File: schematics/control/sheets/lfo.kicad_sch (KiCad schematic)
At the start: 33 parts, among them Q1 BC548C, Q2 BC548C, U1 TL074, U10 TL072, U2 TL072, U9 TL074

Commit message: Added pulse width mod schematics
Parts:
- removed C18: 22n-47n (foil), Capacitor_THT:C_Rect_L7.0mm_W2.5mm_P5.00mm, symbol Device:C
- removed Q2: BC548C, Package_TO_SOT_THT:TO-92L_Inline_Wide, symbol Transistor_BJT:BC548
- removed R18, R19, R21, R23, R25: 100k, Shmoergh_Custom_Footprints:R_Axial_DIN0207_L6.3mm_D2.5mm_P7.62mm_Horizontal, symbol Device:R
- removed R27: 10k, Shmoergh_Custom_Footprints:R_Axial_DIN0207_L6.3mm_D2.5mm_P7.62mm_Horizontal, symbol Device:R
- removed R29, R31: 47k, Shmoergh_Custom_Footprints:R_Axial_DIN0207_L6.3mm_D2.5mm_P7.62mm_Horizontal, symbol Device:R
- removed R33: 1k, Shmoergh_Custom_Footprints:R_Axial_DIN0207_L6.3mm_D2.5mm_P7.62mm_Horizontal, symbol Device:R
- removed RV_PWM_SPEED1: R_Potentiometer_Trim, Potentiometer_THT:Potentiometer_Runtron_RM-065_Vertical, symbol Device:R_Potentiometer_Trim
- removed U1: TL074, Package_DIP:DIP-14_W7.62mm, symbol Amplifier_Operational:TL074
- removed U10, U2: TL072, Package_DIP:DIP-8_W7.62mm, symbol Amplifier_Operational:TL072
- added C29: 470n foil, symbol Device:C
- added R1 (x2): 47k, symbol Device:R
- added R49: 100k, symbol Device:R
- added R50: 220k, symbol Device:R
- added RV1 (x2): 100k, symbol Device:R_Potentiometer_Trim
- added RV_PWM_FREQ2: 1M, symbol Device:R_Potentiometer_Trim
- added SW1: SW_DP3T, symbol Switch:SW_DP3T
- added U11: TL072, symbol Amplifier_Operational:TL072
- added unit 4 of U7
- added unit 3 of U7
- renumbered C13 to C12, C14 to C13, C15 to C14, C16 to C15, C17 to C16, R16 to R29, R17 to R30, R20 to R31, R22 to R32, R24 to R33, R26 to R34, R28 to R35, R30 to R36, R32 to R37, RV_LFO_SPEED2 to RV_LFO_SPEED1, U9 to U7
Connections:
- net +12V: now also R1.2, R1.2, U11.8 (V+)
- net -12V: now also U11.4 (V-)
- net GND: now also RV1.1, RV1.1, SW1.1, SW1.5, SW1.6, U11.3 (+), U11.6 (-), U7.12 (+)
- net PWM_OUT: now also SW1.7
- net at C16.1, U7.1, U7.6 (-): now also U7.10 (+)
- net at R37.2: now also U7.8, U7.9 (-)
- new net: R1.1, RV1.3 (x2)
- new net: RV1.2, SW1.4
- new net: R49.2, R50.1, U11.5 (+)
- new net: R50.2, RV_PWM_FREQ2.2, RV_PWM_FREQ2.3, U11.7
- new net: C29.1, RV_PWM_FREQ2.1, U11.2 (-)
- new net: U7.13 (-), U7.14
- new net: C29.2, R49.1, SW1.8, U11.1
- new net: RV1.2, SW1.2
- new net PULSE_WIDTH: SW1.3
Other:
- note added: "PWM positions: 1. Square 2. Narrow 3. PWM"
- note removed: "The other half of the LFO is in the filter LFO sheet. Should be close to each other on the PCB."
- moved on the sheet: C12, C13, C14, C15, U7E

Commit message: Updated PWM values
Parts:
- added R52: 100k-1M, symbol Device:R
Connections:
- net at R50.2, U11.7: now also R52.2; no longer RV_PWM_FREQ2.2, RV_PWM_FREQ2.3
- new net: R52.1, RV_PWM_FREQ2.2, RV_PWM_FREQ2.3
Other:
- note added: "Slowing PWM even further down"
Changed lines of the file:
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@@
   (junction (at 63.5 172.72) (diameter 0) (color 0 0 0 0)
   )
+  (junction (at 158.75 114.3) (diameter 0) (color 0 0 0 0)
+  )
   (junction (at 36.83 172.72) (diameter 0) (color 0 0 0 0)
   )
@@
   (junction (at 128.27 67.31) (diameter 0) (color 0 0 0 0)
   )
-  (junction (at 158.75 114.3) (diameter 0) (color 0 0 0 0)
-  )
   (junction (at 76.2 180.34) (diameter 0) (color 0 0 0 0)
   )
@@
     (stroke (width 0) (type default))
   )
+  (wire (pts (xy 175.26 114.3) (xy 186.69 114.3))
+    (stroke (width 0) (type default))
+  )
   (wire (pts (xy 86.36 41.91) (xy 99.06 41.91))
     (stroke (width 0) (type default))
@@
     (stroke (width 0) (type default))
   )
+  (wire (pts (xy 158.75 114.3) (xy 167.64 114.3))
+    (stroke (width 0) (type default))
+  )
   (wire (pts (xy 176.53 46.99) (xy 172.72 46.99))
     (stroke (width 0) (type default))
@@
     (stroke (width 0) (type default))
   )
+  (polyline (pts (xy 171.45 102.87) (xy 171.45 107.95))
+    (stroke (width 0) (type dash))
+  )
   (wire (pts (xy 236.22 128.27) (xy 241.3 128.27))
     (stroke (width 0) (type default))
@@
   )
   (wire (pts (xy 236.22 118.11) (xy 241.3 118.11))
-    (stroke (width 0) (type default))
-  )
-  (wire (pts (xy 158.75 114.3) (xy 186.69 114.3))
     (stroke (width 0) (type default))
   )
@@
   )
   (text "PWM positions:\n1. Square\n2. Narrow\n3. PWM" (at 241.3 148.59 0)
+    (effects (font (size 1.27 1.27)) (justify left bottom))
+  )
+  (text "Slowing PWM even further down" (at 149.86 101.6 0)
     (effects (font (size 1.27 1.27)) (justify left bottom))
   )
@@
         )
       )
+    )
+  )
+  (symbol (lib_id "Device:R") (at 171.45 114.3 90) (unit 1)
+    (in_bom yes) (on_board yes) (dnp no) (fields_autoplaced)
+    (property "Reference" "R52" (at 171.45 109.22 90)
+      (effects (font (size 1.27 1.27)))
+    )
+    (property "Value" "100k-1M" (at 171.45 111.76 90)
+      (effects (font (size 1.27 1.27)))
+    )
+    (property "Footprint" "" (at 171.45 116.078 90)
+      (effects (font (size 1.27 1.27)) hide)
+    )
+    (property "Datasheet" "~" (at 171.45 114.3 0)
+      (effects (font (size 1.27 1.27)) hide)
+    )
+    (pin "1")
+    (pin "2")
+    (instances
+      (project "shmoergh-funk-live-control"
+        (path "/6d7b782d-8b2e-4b40-a99f-4bf41187d978/2e981da9-3fd3-40a6-a1fb-543bdfad6423"
+          (reference "R52") (unit 1)
+        )
+      )

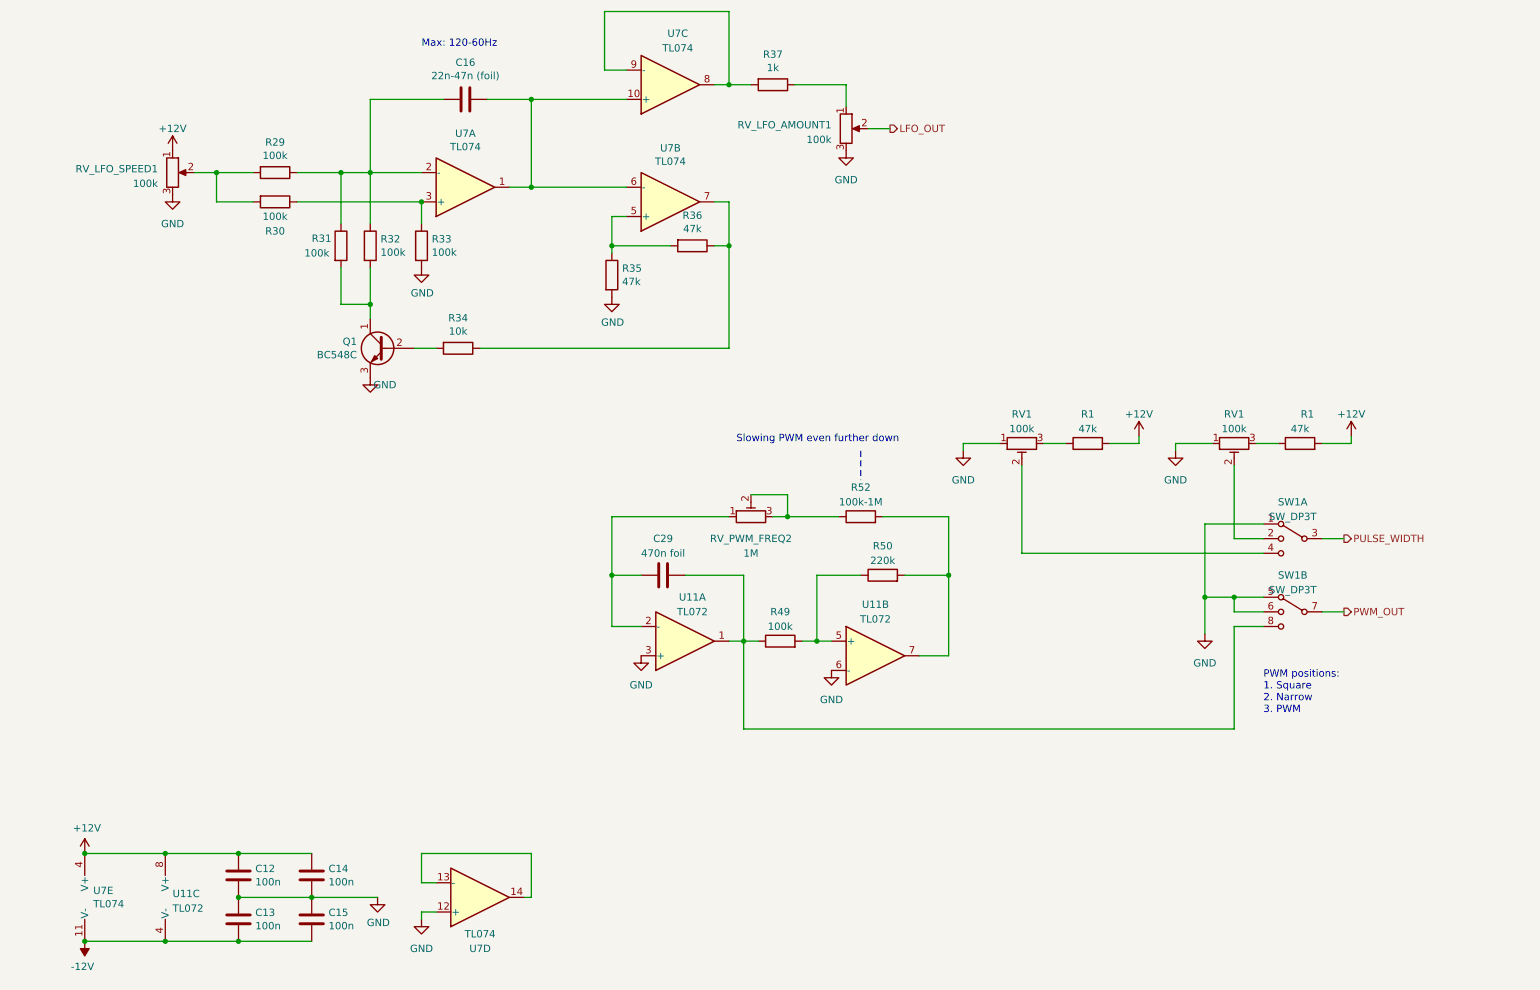
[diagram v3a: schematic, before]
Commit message: Added all UI components to schematics
- digital UI
- filter UI
- updated voice interface connection
- simplified schematics a lot
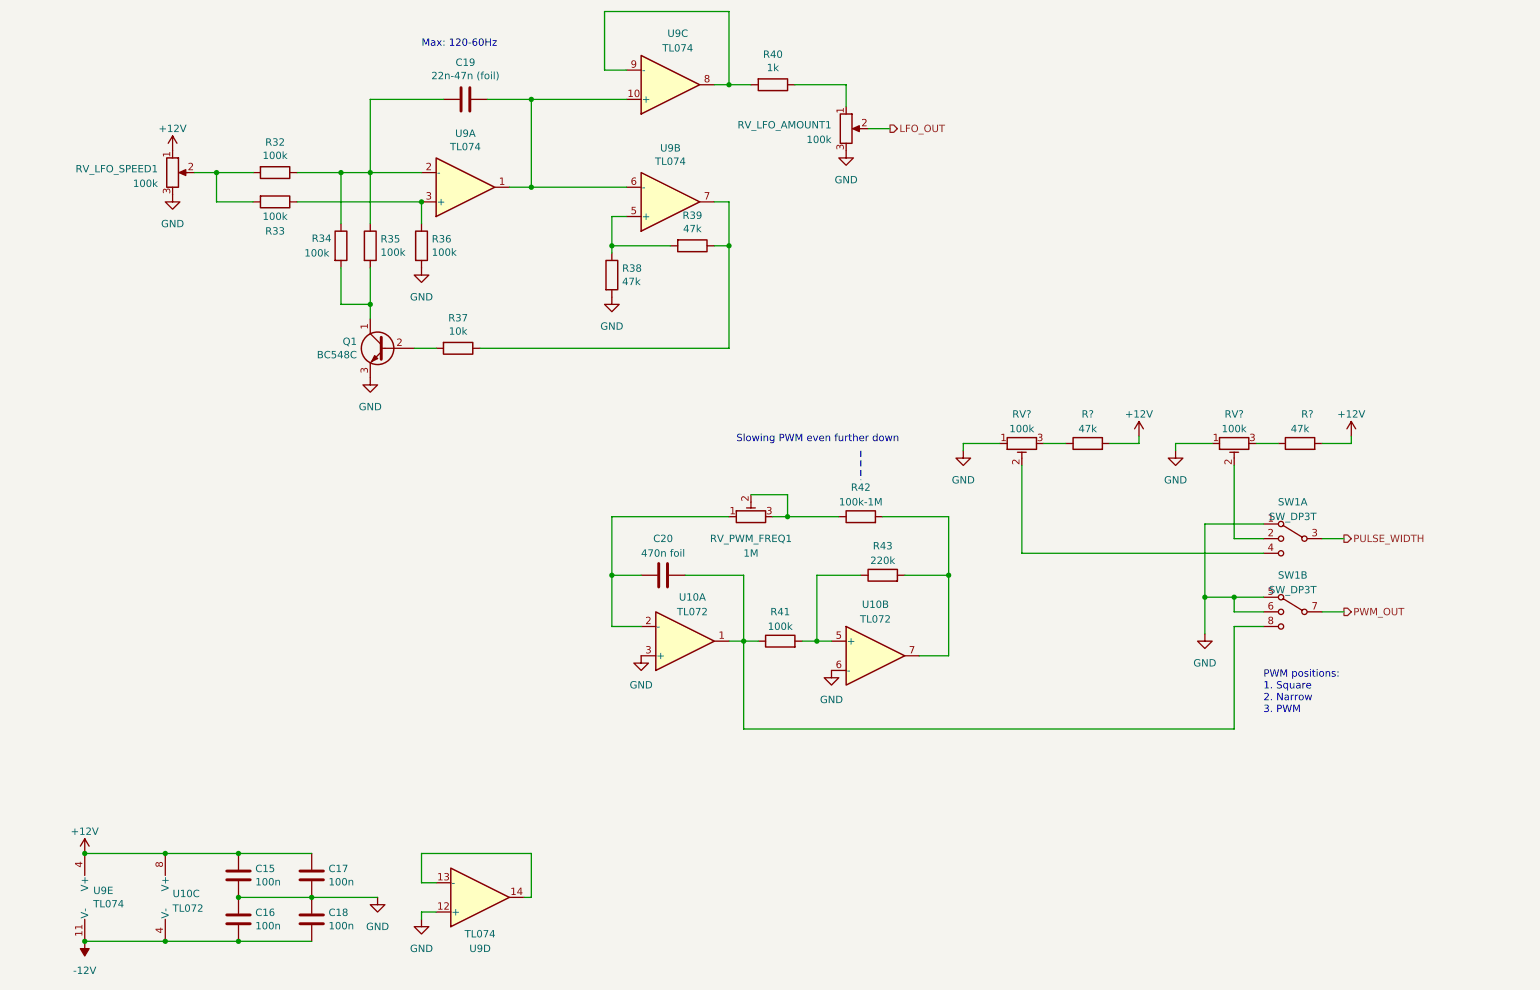
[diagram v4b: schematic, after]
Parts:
- C15: renamed from C12; footprint Capacitor_THT:C_Disc_D3.0mm_W2.0mm_P2.50mm -> (none)
- C16: renamed from C13; footprint Capacitor_THT:C_Disc_D3.0mm_W2.0mm_P2.50mm -> (none)
- C17: renamed from C14; footprint Capacitor_THT:C_Disc_D3.0mm_W2.0mm_P2.50mm -> (none)
- C18: renamed from C15; footprint Capacitor_THT:C_Disc_D3.0mm_W2.0mm_P2.50mm -> (none)
- C19: renamed from C16; footprint Capacitor_THT:C_Rect_L7.0mm_W2.5mm_P5.00mm -> (none)
- Q1: footprint Package_TO_SOT_THT:TO-92L_Inline_Wide -> (none)
- R32: renamed from R29; footprint Shmoergh_Custom_Footprints:R_Axial_DIN0207_L6.3mm_D2.5mm_P7.62mm_Horizontal -> (none)
- R33: renamed from R30; footprint Shmoergh_Custom_Footprints:R_Axial_DIN0207_L6.3mm_D2.5mm_P7.62mm_Horizontal -> (none)
- R34: renamed from R31; footprint Shmoergh_Custom_Footprints:R_Axial_DIN0207_L6.3mm_D2.5mm_P7.62mm_Horizontal -> (none)
- R35: renamed from R32; footprint Shmoergh_Custom_Footprints:R_Axial_DIN0207_L6.3mm_D2.5mm_P7.62mm_Horizontal -> (none)
- R36: renamed from R33; footprint Shmoergh_Custom_Footprints:R_Axial_DIN0207_L6.3mm_D2.5mm_P7.62mm_Horizontal -> (none)
- R37: renamed from R34; footprint Shmoergh_Custom_Footprints:R_Axial_DIN0207_L6.3mm_D2.5mm_P7.62mm_Horizontal -> (none)
- R38: renamed from R35; footprint Shmoergh_Custom_Footprints:R_Axial_DIN0207_L6.3mm_D2.5mm_P7.62mm_Horizontal -> (none)
- R39: renamed from R36; footprint Shmoergh_Custom_Footprints:R_Axial_DIN0207_L6.3mm_D2.5mm_P7.62mm_Horizontal -> (none)
- R40: renamed from R37; footprint Shmoergh_Custom_Footprints:R_Axial_DIN0207_L6.3mm_D2.5mm_P7.62mm_Horizontal -> (none)
- RV_LFO_AMOUNT1, RV_LFO_SPEED1: footprint Shmoergh_Custom_Footprints:NSL25_01x03_Vertical -> (none)
- U9: renamed from U7; footprint Package_DIP:DIP-14_W7.62mm -> (none)
- renumbered C29 to C20, R49 to R41, R52 to R42, R50 to R43, R1 to R?, RV1 to RV?, RV_PWM_FREQ2 to RV_PWM_FREQ1, U11 to U10, U7 to U9

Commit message: Schemo work
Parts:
- C15, C16, C17, C18: footprint (none) -> Capacitor_THT:C_Disc_D3.0mm_W2.0mm_P2.50mm
- C19, C20: footprint (none) -> Capacitor_THT:C_Rect_L7.0mm_W3.5mm_P5.00mm
- Q1: footprint (none) -> PCM_Package_TO_SOT_THT_AKL:TO-92_Inline_Wide
- R32, R33, R34, R35, R36, R37, R38, R39, R40, R41, R42, R43, R? (x2): footprint (none) -> Shmoergh_Custom_Footprints:R_Axial_DIN0207_L6.3mm_D2.5mm_P7.62mm_Horizontal
- RV? (x2), RV_PWM_FREQ1: footprint (none) -> Potentiometer_THT:Potentiometer_Runtron_RM-065_Vertical
- RV_LFO_AMOUNT1, RV_LFO_SPEED1: footprint (none) -> Shmoergh_Custom_Footprints:NSL25_01x03_Vertical
- SW1: footprint (none) -> Shmoergh_Custom_Footprints:NSL25_01x08_Vertical
- U10: footprint (none) -> PCM_Package_DIP_AKL:DIP-8_W7.62mm_LongPads
- U9: footprint (none) -> PCM_Package_DIP_AKL:DIP-14_W7.62mm_LongPads

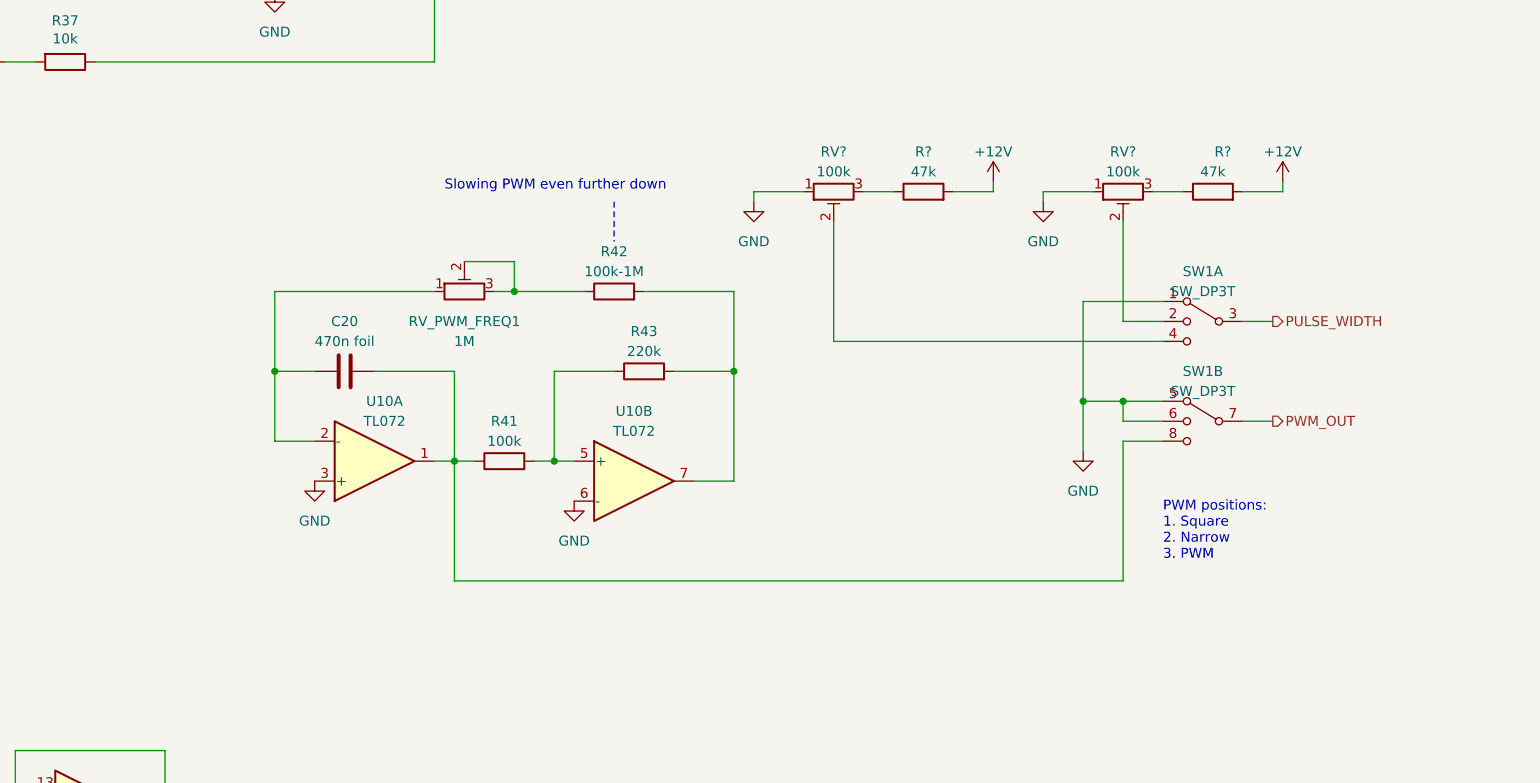
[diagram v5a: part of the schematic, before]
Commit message: Simplified PWM switch IO
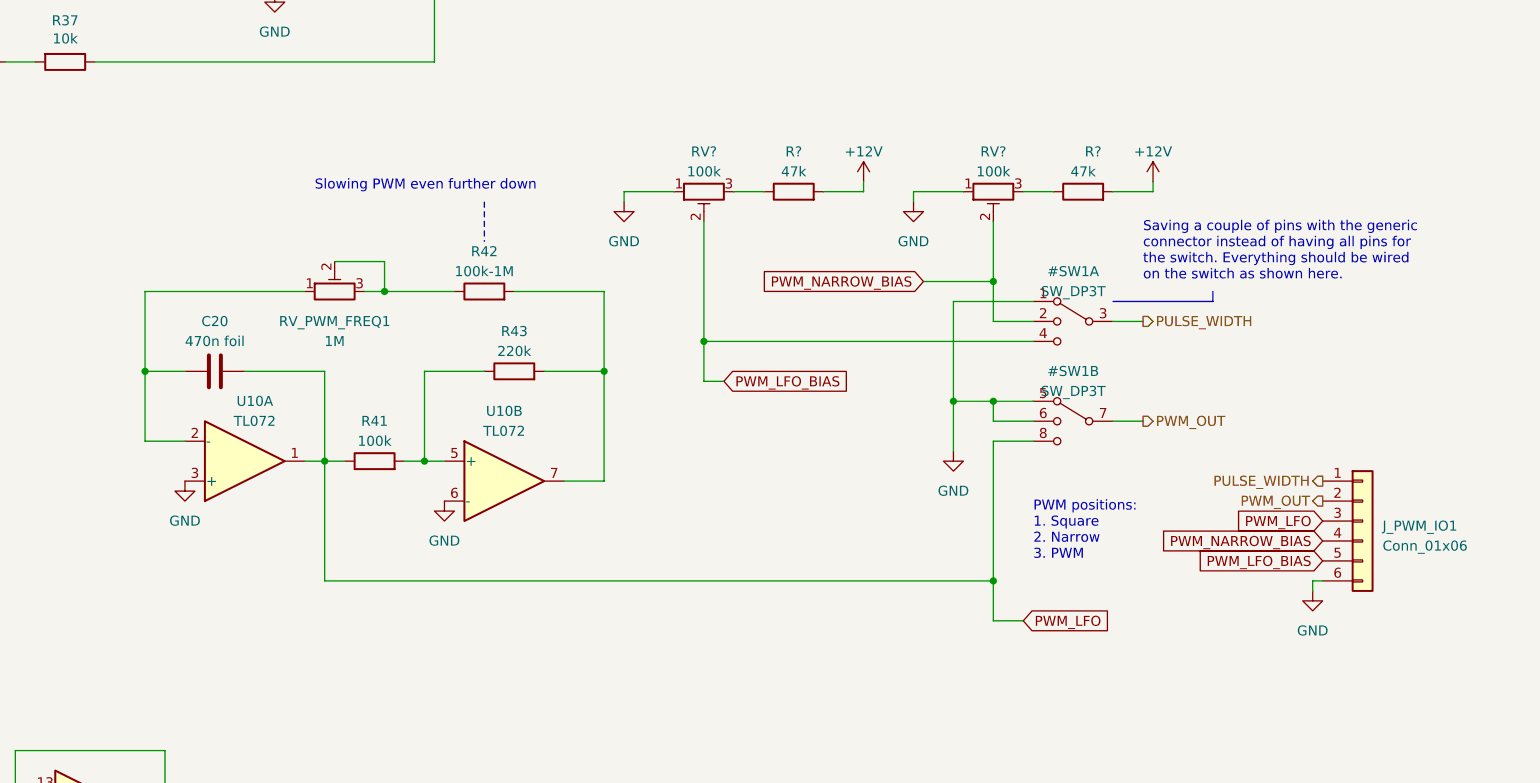
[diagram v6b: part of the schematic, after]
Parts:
- added J_PWM_IO1: Conn_01x06, Shmoergh_Custom_Footprints:NSL25_01x06_Vertical, symbol Connector_Generic:Conn_01x06
- renumbered SW1 to #SW1
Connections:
- net GND: now also J_PWM_IO1.6 (Pin_6)
- net PULSE_WIDTH: now also J_PWM_IO1.1 (Pin_1)
- net PWM_OUT: now also J_PWM_IO1.2 (Pin_2)
- net PWM_LFO_BIAS: now reaches #SW1.4, RV?.2
- net PWM_LFO_BIAS: now also J_PWM_IO1.5 (Pin_5)
- net PWM_LFO: now reaches #SW1.8, C20.2, R41.1, U10.1
- net PWM_LFO: now also J_PWM_IO1.3 (Pin_3)
- net PWM_NARROW_BIAS: now reaches #SW1.2, RV?.2
- net PWM_NARROW_BIAS: now also J_PWM_IO1.4 (Pin_4)
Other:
- note added: "Saving a couple of pins with the generic connector instead of having all pins for the switch. Everything should be wired on the switch as shown here."
- moved on the sheet: C20, R41, R42, R43, R?, RV?, RV_PWM_FREQ1, U10A, U10B
